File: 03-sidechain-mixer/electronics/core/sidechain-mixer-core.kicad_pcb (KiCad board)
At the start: 2 copper layers, 58 x 110 mm, 23 parts, among them J1 Conn_01x04, J2 Conn_02x05_Odd_Even, J3 Conn_02x05_Odd_Even, J4 Conn_01x02, J5 Conn_02x03_Odd_Even, J6 Conn_02x02_Counter_Clockwise, J8 Conn_01x06, U7 TL072

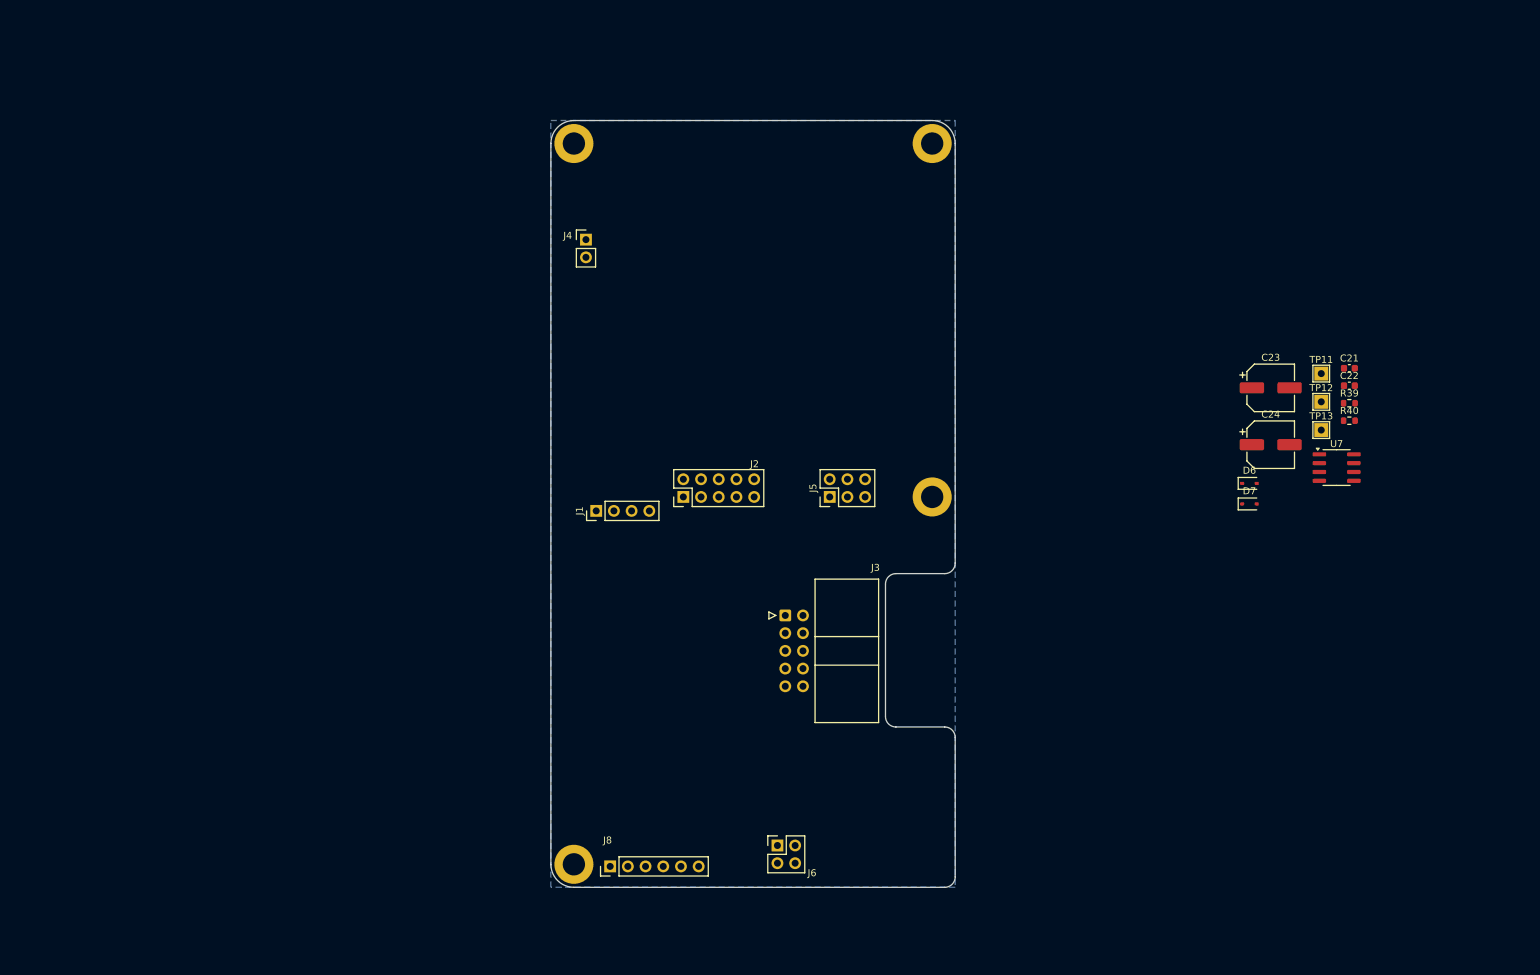
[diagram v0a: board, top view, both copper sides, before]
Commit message: Prepared sidechain mixer PCB
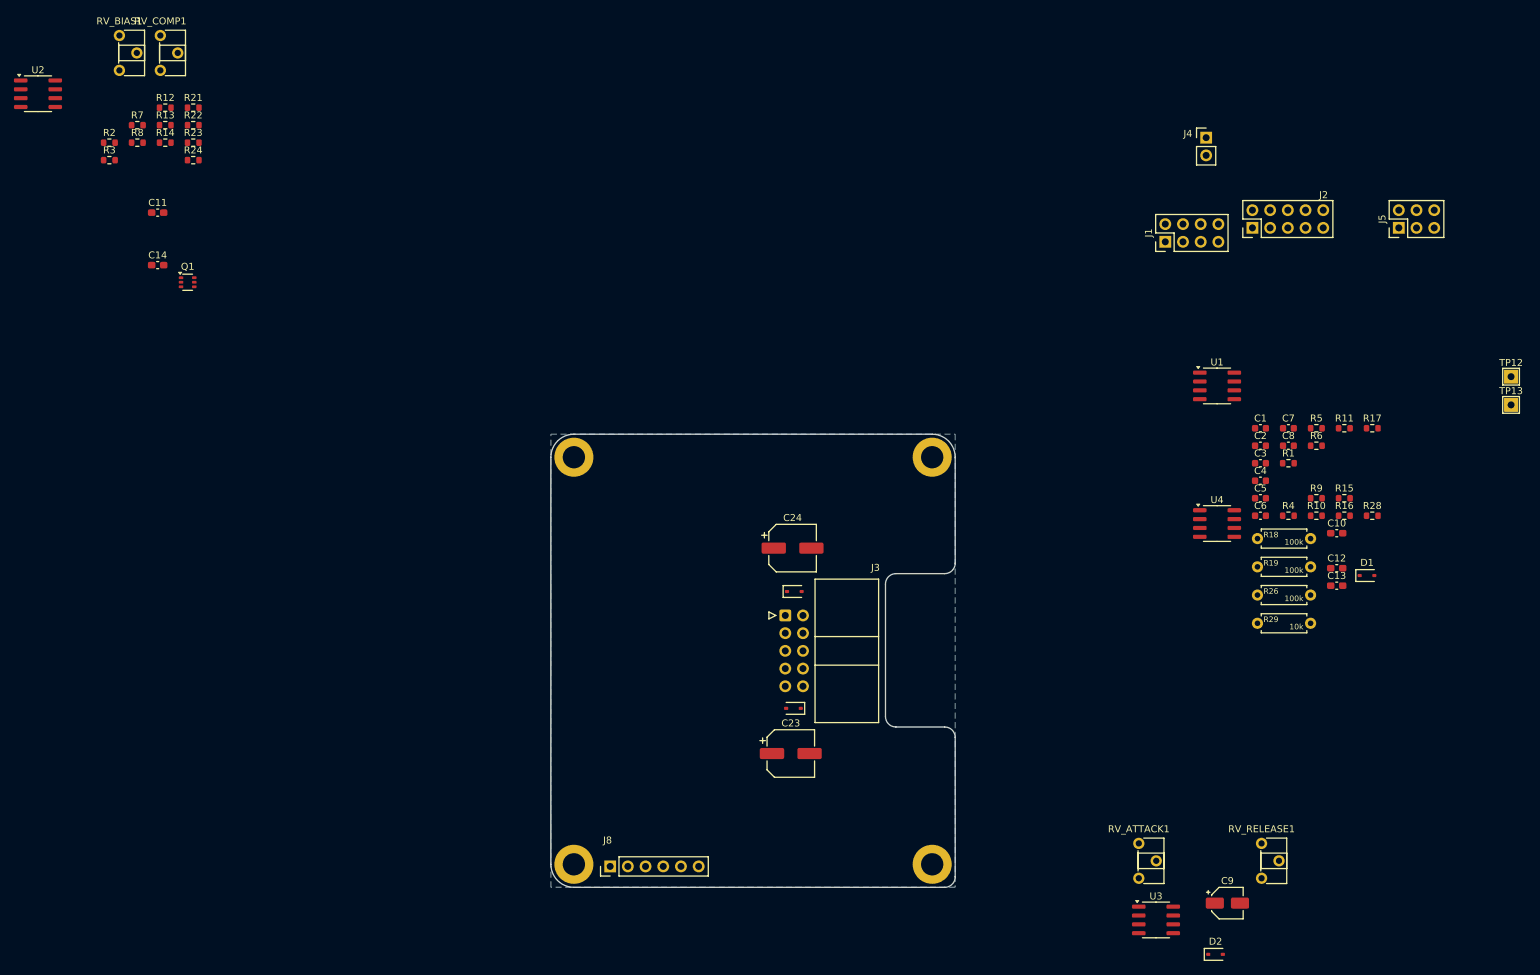
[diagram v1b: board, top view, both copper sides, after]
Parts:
- removed C21, C22: 100n, Capacitor_SMD:C_0603_1608Metric
- removed J6: Conn_02x02_Counter_Clockwise, Connector_PinHeader_2.54mm:PinHeader_2x02_P2.54mm_Vertical
- removed R39: 240k, Resistor_SMD:R_0603_1608Metric
- removed R40: 100k, Resistor_SMD:R_0603_1608Metric
- removed TP11: -5V, TestPoint:TestPoint_THTPad_2.0x2.0mm_Drill1.0mm
- removed U7: TL072, Package_SO:SOIC-8_3.9x4.9mm_P1.27mm
- added C1: 100n, Capacitor_SMD:C_0603_1608Metric, F.Cu at (225.8, 88.1)
- added C10: 47p, Capacitor_SMD:C_0603_1608Metric_Pad1.08x0.95mm_HandSolder, F.Cu at (236.7, 103.2)
- added C11: 47p, Capacitor_SMD:C_0603_1608Metric_Pad1.08x0.95mm_HandSolder, F.Cu at (67.6, 57.2)
- added C12: 47p, Capacitor_SMD:C_0603_1608Metric_Pad1.08x0.95mm_HandSolder, F.Cu at (236.7, 108.2)
- added C13: 47p, Capacitor_SMD:C_0603_1608Metric_Pad1.08x0.95mm_HandSolder, F.Cu at (236.7, 110.7)
- added C14: 47p, Capacitor_SMD:C_0603_1608Metric_Pad1.08x0.95mm_HandSolder, F.Cu at (67.6, 64.7)
- added C2: 100n, Capacitor_SMD:C_0603_1608Metric, F.Cu at (225.8, 90.7)
- added C3: 100n, Capacitor_SMD:C_0603_1608Metric, F.Cu at (225.8, 93.2)
- added C4: 100n, Capacitor_SMD:C_0603_1608Metric, F.Cu at (225.8, 95.7)
- added C5: 100n, Capacitor_SMD:C_0603_1608Metric, F.Cu at (225.8, 98.2)
- added C6: 100n, Capacitor_SMD:C_0603_1608Metric, F.Cu at (225.8, 100.7)
- added C7: 100n, Capacitor_SMD:C_0603_1608Metric, F.Cu at (229.8, 88.1)
- added C8: 100n, Capacitor_SMD:C_0603_1608Metric, F.Cu at (229.8, 90.7)
- added C9: 10u, Capacitor_SMD:CP_Elec_4x5.4, F.Cu at (221.1, 156.3)
- added D1: 1N4148, Diode_SMD:D_SOD-323, F.Cu at (241.1, 109.3)
- added D2: 1N4148, Diode_SMD:D_SOD-323, F.Cu at (219.3, 163.6)
- added Q1: BC847BS, Package_TO_SOT_SMD:SOT-363_SC-70-6, F.Cu at (71.9, 67.2)
- added R1: 100k, Resistor_SMD:R_0603_1608Metric, F.Cu at (229.8, 93.2)
- added R10: 100k, Resistor_SMD:R_0603_1608Metric, F.Cu at (233.8, 100.7)
- added R11: 1k, Resistor_SMD:R_0603_1608Metric, F.Cu at (237.8, 88.1)
- added R12: 10k, Resistor_SMD:R_0603_1608Metric, F.Cu at (68.7, 42.2)
- added R13: 33k, Resistor_SMD:R_0603_1608Metric, F.Cu at (68.7, 44.7)
- added R14: 200k, Resistor_SMD:R_0603_1608Metric, F.Cu at (68.7, 47.2)
- added R15: 200k, Resistor_SMD:R_0603_1608Metric, F.Cu at (237.8, 98.2)
- added R16: 100k, Resistor_SMD:R_0603_1608Metric, F.Cu at (237.8, 100.7)
- added R17: 100k, Resistor_SMD:R_0603_1608Metric, F.Cu at (241.8, 88.1)
- added R18: 100k, Shmoergh_Custom_Footprints:R_Axial_DIN0207_L6.3mm_D2.5mm_P7.62mm_Horizontal, F.Cu at (225.4, 104.0)
- added R19: 100k, Shmoergh_Custom_Footprints:R_Axial_DIN0207_L6.3mm_D2.5mm_P7.62mm_Horizontal, F.Cu at (225.4, 108.0)
- added R2: 100k, Resistor_SMD:R_0603_1608Metric, F.Cu at (60.7, 47.2)
- added R21: 10k, Resistor_SMD:R_0603_1608Metric, F.Cu at (72.7, 42.2)
- added R22: 10k, Resistor_SMD:R_0603_1608Metric, F.Cu at (72.7, 44.7)
- added R23: 470k, Resistor_SMD:R_0603_1608Metric, F.Cu at (72.7, 47.2)
- added R24: 470k, Resistor_SMD:R_0603_1608Metric, F.Cu at (72.7, 49.7)
- added R26: 100k, Shmoergh_Custom_Footprints:R_Axial_DIN0207_L6.3mm_D2.5mm_P7.62mm_Horizontal, F.Cu at (225.4, 112.1)
- added R28: 100k, Resistor_SMD:R_0603_1608Metric, F.Cu at (241.8, 100.7)
- added R29: 10k, Shmoergh_Custom_Footprints:R_Axial_DIN0207_L6.3mm_D2.5mm_P7.62mm_Horizontal, F.Cu at (225.4, 116.1)
- added R3: 100k, Resistor_SMD:R_0603_1608Metric, F.Cu at (60.7, 49.7)
- added R4: 100k, Resistor_SMD:R_0603_1608Metric, F.Cu at (229.8, 100.7)
- added R5: 100k, Resistor_SMD:R_0603_1608Metric, F.Cu at (233.8, 88.1)
- added R6: 100k, Resistor_SMD:R_0603_1608Metric, F.Cu at (233.8, 90.7)
- added R7: 100k, Resistor_SMD:R_0603_1608Metric, F.Cu at (64.7, 44.7)
- added R8: 220, Resistor_SMD:R_0603_1608Metric, F.Cu at (64.7, 47.2)
- added R9: 100k, Resistor_SMD:R_0603_1608Metric, F.Cu at (233.8, 98.2)
- added RV_ATTACK1: 10-100k, Potentiometer_THT:Potentiometer_ACP_CA6-H2,5_Horizontal, F.Cu at (208.3, 147.7)
- added RV_BIAS1: 100k, Potentiometer_THT:Potentiometer_ACP_CA6-H2,5_Horizontal, F.Cu at (62.1, 31.8)
- added RV_COMP1: 10k, Potentiometer_THT:Potentiometer_ACP_CA6-H2,5_Horizontal, F.Cu at (68.0, 31.8)
- added RV_RELEASE1: 10-100k, Potentiometer_THT:Potentiometer_ACP_CA6-H2,5_Horizontal, F.Cu at (225.9, 147.7)
- added U1: TL072, Package_SO:SOIC-8_3.9x4.9mm_P1.27mm, F.Cu at (219.6, 82.1)
- added U2: TL072, Package_SO:SOIC-8_3.9x4.9mm_P1.27mm, F.Cu at (50.4, 40.2)
- added U3: TL072, Package_SO:SOIC-8_3.9x4.9mm_P1.27mm, F.Cu at (210.8, 158.7)
- added U4: TL072, Package_SO:SOIC-8_3.9x4.9mm_P1.27mm, F.Cu at (219.6, 101.8)
- J1: value Conn_01x04 -> Conn_02x04_Odd_Even; footprint Connector_PinHeader_2.54mm:PinHeader_1x04_P2.54mm_Vertical -> Connector_PinHeader_2.54mm:PinHeader_2x04_P2.54mm_Vertical
- moved J1 90.3 mm to (212.1, 61.4)
- moved J2 90.3 mm to (224.6, 59.4)
- moved J5 90.3 mm to (245.6, 59.4)
- moved J4 90.2 mm to (218.0, 46.5)
- moved C23 86.6 mm to (158.4, 134.8)
- moved D6 72.9 mm to (158.8, 128.3), turned to 180 degrees
- moved C24 70.2 mm to (158.7, 105.3)
- moved D7 66.5 mm to (158.9, 111.6)
- moved H2 52.7 mm to (178.7, 150.7)
- moved H1 45.0 mm to (127.3, 92.3)
- moved H4 45.0 mm to (178.7, 92.3)
- moved TP12 27.5 mm to (261.7, 80.7)
- moved TP13 27.5 mm to (261.7, 84.8)
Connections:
- J1 pad 1: CV -> RATIO_1
- J1 pad 2: HARD_SYNC -> CH_4_GAIN_1
- J1 pad 3: FM -> RATIO_3
- J1 pad 4: SQR_SHAPE -> CH_4_GAIN_3_VOL_3
- J2 pad 1: RAW_SAW -> IN_1
- J2 pad 3: SQR -> IN_2
- J2 pad 5: TRI -> IN_3
- J2 pad 7: SAW -> IN_4
- J2 pad 9: SAW_INV -> OUT
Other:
- board size 58 x 110 mm -> 58 x 65 mm

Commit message: SC-Mixer PCB base done
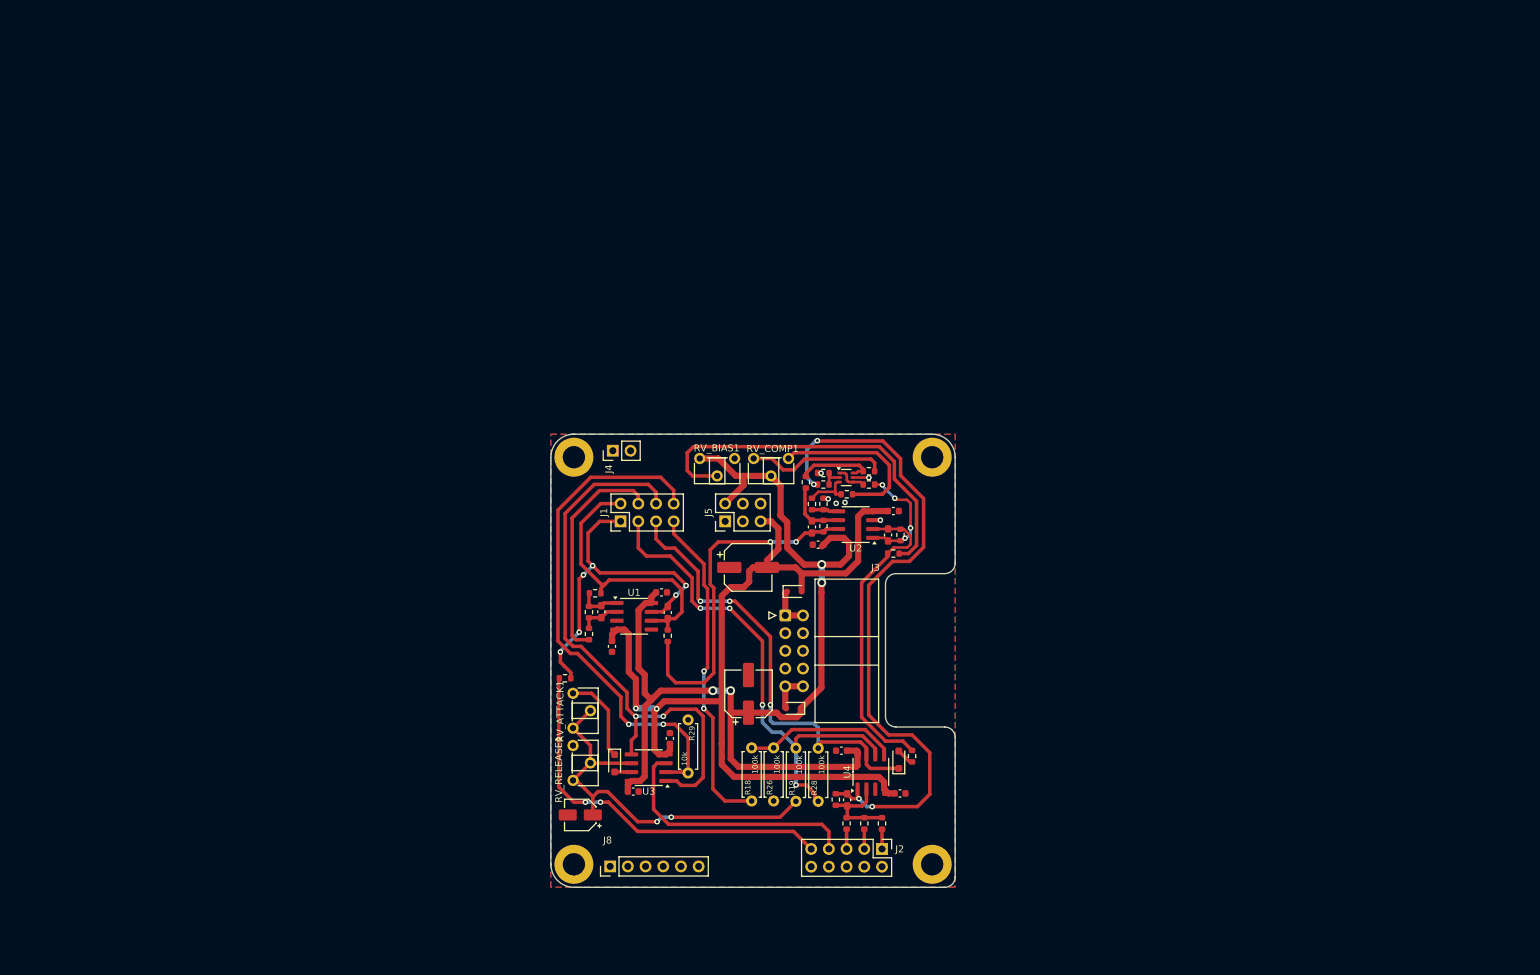
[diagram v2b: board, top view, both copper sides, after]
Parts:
- removed TP12: 12V, TestPoint:TestPoint_THTPad_2.0x2.0mm_Drill1.0mm
- removed TP13: -12V, TestPoint:TestPoint_THTPad_2.0x2.0mm_Drill1.0mm
- D1, D2: footprint Diode_SMD:D_SOD-323 -> Diode_SMD:D_SOD-323_HandSoldering
- R28: footprint Resistor_SMD:R_0603_1608Metric -> Shmoergh_Custom_Footprints:R_Axial_DIN0207_L6.3mm_D2.5mm_P7.62mm_Horizontal
- moved U2 132.6 mm to (167.7, 102.0), turned to 180 degrees
- moved R13 120.7 mm to (174.1, 103.5), turned to -90 degrees
- moved R14 119.9 mm to (173.1, 106.1), turned to 180 degrees
- moved R2 118.7 mm to (169.6, 94.3)
- moved R11 117.4 mm to (126.0, 124.0), turned to 180 degrees
- moved R3 116.1 mm to (166.4, 97.6)
- moved R17 115.4 mm to (129.5, 114.5), turned to 90 degrees
- moved R12 114.5 mm to (169.6, 96.2), turned to 180 degrees
- moved C14 111.7 mm to (172.4, 103.5), turned to -90 degrees
- moved R7 111.1 mm to (163.1, 96.2)
- moved R16 109.7 mm to (129.5, 117.7), turned to 90 degrees
- moved R8 109.2 mm to (163.1, 94.6)
- moved RV_COMP1 108.6 mm to (158.1, 92.5), turned to -90 degrees
- moved RV_BIAS1 107.1 mm to (150.4, 92.5), turned to -90 degrees
- moved R23 105.8 mm to (163.1, 102.2), turned to -90 degrees
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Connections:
- J1 pad 1: RATIO_1 -> MAIN_VOL_3
- J1 pad 2: CH_4_GAIN_1 -> MAIN_VOL_1
- J1 pad 3: RATIO_3 -> RATIO_1
- J1 pad 4: CH_4_GAIN_3_VOL_3 -> CH_4_VOL_2
- J1 pad 5: THRESHOLD -> RATIO_3
- J1 pad 6: CH_4_VOL_2 -> CH_4_GAIN_3_VOL_3
- J1 pad 7: MAIN_VOL_1 -> THRESHOLD
- J1 pad 8: MAIN_VOL_3 -> CH_4_GAIN_1
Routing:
- net +12V: track 0.00 -> 154.9 mm, vias 0 -> 4
- net -12V: track 0.00 -> 134.9 mm, vias 0 -> 2
- net Net-(C10-Pad2): track 0.00 -> 97.2 mm, vias 0 -> 4
- net CH_4_GAIN_3_VOL_3: track 0.00 -> 82.0 mm, vias 0 -> 2
- net CH_4_GAIN_1: track 0.00 -> 74.4 mm, vias 0 -> 2
- net RATIO_1: track 0.00 -> 71.6 mm, vias 0 -> 4
- net RATIO_3: track 0.00 -> 64.5 mm, vias 0 -> 3
- net Net-(U3B--): track 0.00 -> 57.9 mm, vias 0 -> 2
- net OUT: track 0.00 -> 55.5 mm, vias 0 -> 2
- net Net-(R14-Pad1): track 0.00 -> 54.4 mm
- net MAIN_VOL_3: track 0.00 -> 50.5 mm, vias 0 -> 6
- net Net-(C11-Pad2): track 0.00 -> 49.9 mm, vias 0 -> 2
- net THRESHOLD: track 0.00 -> 47.4 mm, vias 0 -> 2
- net Net-(U2A--): track 0.00 -> 45.1 mm
- net MAIN_VOL_1: track 0.00 -> 40.5 mm
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- added copper zone on F.Cu, net GND

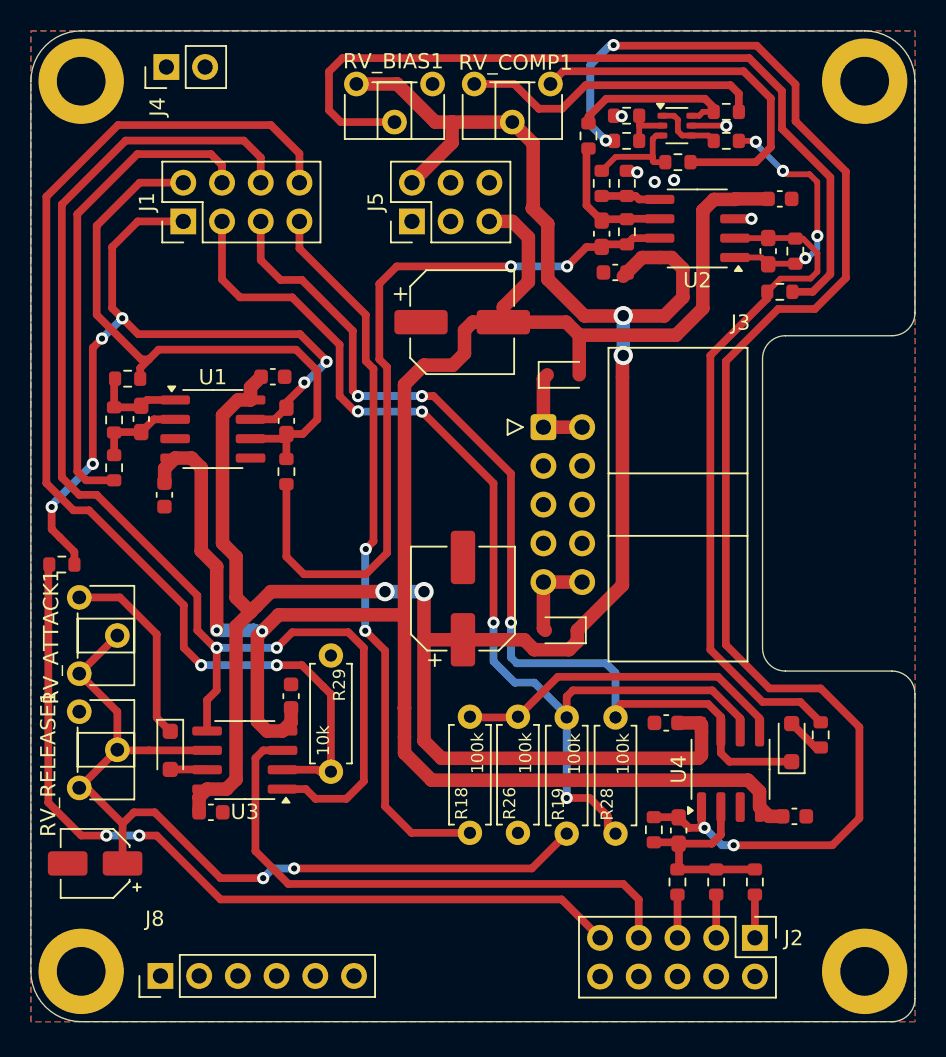
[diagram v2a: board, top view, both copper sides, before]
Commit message: SC-Mixer PCB updates
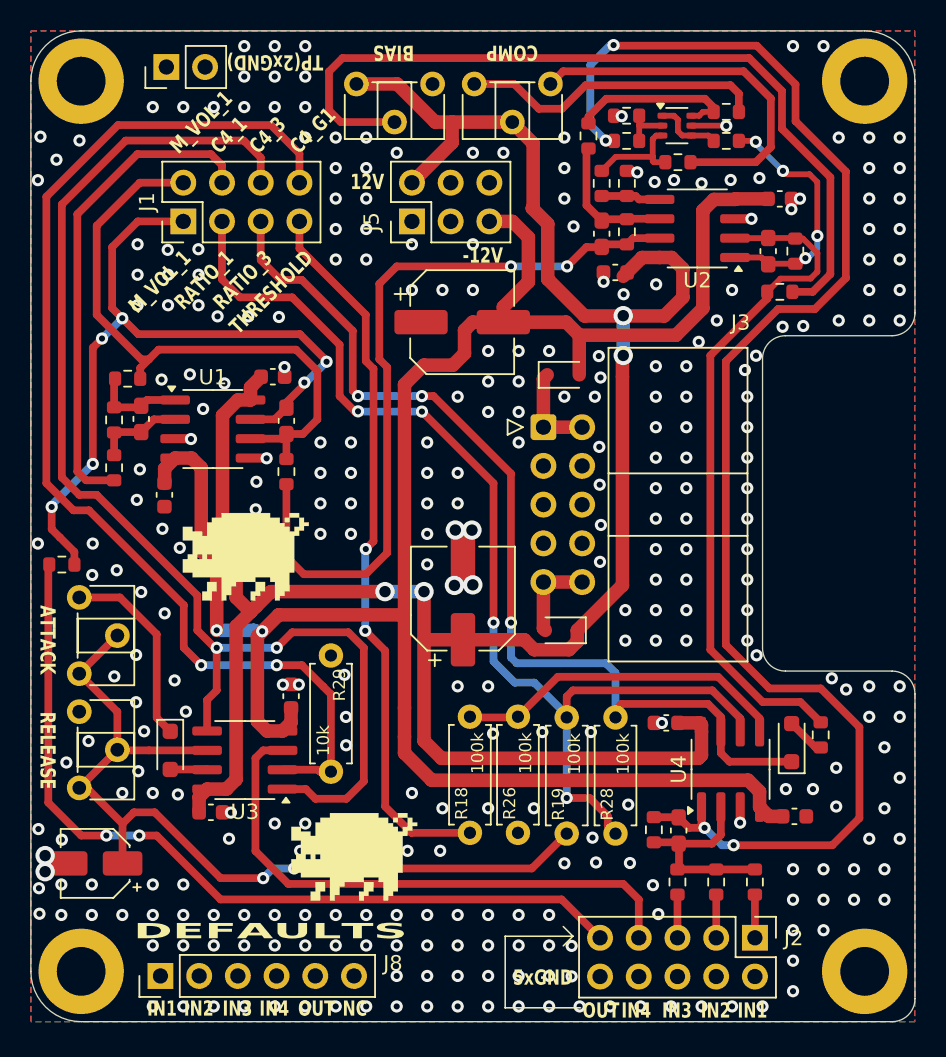
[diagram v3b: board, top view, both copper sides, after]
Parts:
- added G***: LOGO, Shmoergh_Logo:Gyeszno, F.Cu at (138.1, 123.5)
- added G***: LOGO, Shmoergh_Logo:Gyeszno, F.Cu at (145.2, 143.2)
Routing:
- net GND: vias 6 -> 322
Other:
- board text added: "-12V"
- board text added: "12V"
- board text added: "5xGND"
- board text added: "ATTACK"
- board text added: "BIAS"
- board text added: "C4_1"
- board text added: "C4_3"
- board text added: "C4_G1"
- board text added: "COMP"
- board text added: "DEFAULTS"
- board text added: "IN1"
- board text added: "IN2"
- board text added: "IN3"
- board text added: "IN4"
- board text added: "M_VOL_1"
- board text added: "NC"
- board text added: "OUT"
- board text added: "RATIO_1"
- board text added: "RATIO_3"
- board text added: "RELEASE"
- board text added: "THRESHOLD"
- board text added: "TP(2xGND)"

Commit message: SC-Mixer PCB updates
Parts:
- added G***: LOGO, Shmoergh_Logo:Gyeszno, B.Cu at (149.9, 110.4)
- added G***: LOGO, Shmoergh_Logo:Gyeszno, B.Cu at (167.3, 101.7)
- added G***: LOGO, Shmoergh_Logo:Gyeszno, B.Cu at (171.1, 134.7)
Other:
- board text added: "5x GND"
- board text added: "CH4_1"
- board text added: "CH4_3"
- board text added: "HM-03 Sidechain Mixer V0.1 / 2025 Aug"
- board text added: "M_V_3"
- board text added: "POWER"
- board text added: "RAT_1"
- board text added: "RAT_3"
- board text added: "SHMØERGH HOG MODULEUR"
- board text added: "THRS"
